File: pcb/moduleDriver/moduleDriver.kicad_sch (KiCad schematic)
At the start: 52 parts, among them J10 Sensor, J11 Power, J12 Power, J7 Sensor, J8 Sensor, J9 Sensor

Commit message: yep, this is the winner
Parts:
- removed D?: WS2812B, LED_SMD:LED_WS2812B_PLCC4_5.0x5.0mm_P3.2mm, symbol LED:WS2812B
- removed D?: LED, LED_SMD:LED_0603_1608Metric, symbol Device:LED_Small
- removed J? (x4): I2C, Connector_PinHeader_2.54mm:PinHeader_1x03_P2.54mm_Vertical, symbol Connector:Conn_01x03_Male
- removed R? (x16): 4.7k, Resistor_SMD:R_0603_1608Metric, symbol Device:R_Small
- removed R?: 1.2k, Resistor_SMD:R_0603_1608Metric, symbol Device:R_Small
- removed R? (x2): 2.2k, Resistor_SMD:R_0603_1608Metric, symbol Device:R_Small
- removed SW? (x2): SW_DIP_x08, symbol Switch:SW_DIP_x08
- added D?: LED, LED_SMD:LED_0603_1608Metric, symbol Device:LED_Small
- added J? (x2): I2C, Connector_PinHeader_2.54mm:PinHeader_1x03_P2.54mm_Vertical, symbol Connector:Conn_01x03_Male
- added R?: 1.2k, Resistor_SMD:R_0603_1608Metric, symbol Device:R_Small
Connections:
- net I2C_PULLUP is gone; now on net URART_LR_TX: U?.26 (GPIO20)
- net SCL is gone; now on net UART_RL_RX: U?.25 (GPIO19)
- net SDA is gone; now on net UART_LR_RX: U?.24 (GPIO18)
- net GND: now also D?.1 (K), J?.1 (Pin_1), J?.1 (Pin_1)
- net UART_LR_RX: now also J?.3 (Pin_3)
- net UART_RL_RX: now also J?.2 (Pin_2)
- net UART_RL_TX: now also U?.22 (GPIO17), J?.2 (Pin_2)
- net URART_LR_TX: now also J?.3 (Pin_3)
- net at U?.27 (GPIO21): now also R?.1
- new net: D?.2 (A), R?.2
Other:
- note added: "UART to other modules"
- note removed: "I hate the DIP switches... How about we use a serially chained UART instead of I2C. Or for that matter, use exactly the neopixel protocol! Each module shows up as a neopixel! Ooh, I like it. That way you can not only chain these modules together, but interchageably sequence together neopixels and displays :-) Back to needing 3.3 <-> 5V voltage level translation, but it's kinda neat Hmmmm... but t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"
- note removed: "I think this is the winning strategy"
- note removed: "I2C to other modules"
- note removed: "MASTER SELECT"
- note removed: "MODULE SELECT"
- note removed: "One module should be set to address 0 via the DIP switches. The master module will turn on GPIO20 (I2C_PULLUP), to power the I2C bus. All other modules will have I2C_PULLUP in a High-Z state"
- note removed: "Or... do this with UARTS"
- note removed: "other options instead of DIP switches:"
- moved on the sheet: H1, H3

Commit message: checking voltage levels. Everythign looks correct
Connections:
- net UART_LR_RX: now also U?.26 (GPIO20); no longer U?.24 (GPIO18)
- net UART_RL_RX: now also U?.22 (GPIO17); no longer U?.25 (GPIO19)
- net UART_RL_TX: now also U?.25 (GPIO19); no longer U?.22 (GPIO17)
- net URART_LR_TX: now also U?.24 (GPIO18); no longer U?.26 (GPIO20)
- net LED: now reaches R?.1, U?.27 (GPIO21)
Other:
- note added: "The 2803 says "for 5V CMOS", but the datasheet says anything more than 2.8V is "on" so we should be good. Hi-z or LOW is OFF > 2.8V is ON"
- note added: "The PICO that doesn't receive anything on UART_LR_RX is the master. Benefits: * zero hardware configuration. The start of the chain automatically the master * the signal is rebuffered at each module. * push-push drivers -- not reliant on pullups, which can receive noise a little more than push-push drivers"
- note removed: "Requires 2 TX uarts on the PICO and 2 RX uarts on the PICO. Also, The PICO that doesn't receive anything on UART_LR_RX is the master. Benefits: * zero hardware configuration. The start of the chain automatically the master * the signal is rebuffered at each module. * push-push drivers -- not reliant on pullups, which can receive noise a little more than push-push drivers"
- moved on the sheet: D?, J?, R?, U?

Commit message: Restarting layout
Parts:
- U1: renamed from U?; footprint Package_TO_SOT_SMD:TO-252-3_TabPin2 -> Package_TO_SOT_SMD:TO-252-2; Comment (none) -> Extended; LCSC# (none) -> C83632
- U2: renamed from U?; Comment (none) -> -
- U3, U4: renamed from U?; footprint (none) -> Package_SO:SOP-18_7x12.5mm_P1.27mm; Comment (none) -> Extended; LCSC# (none) -> C181731
- gave numbers to parts that had none: 13
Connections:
- no-connect marks 0 -> 7
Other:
- moved on the sheet: C4

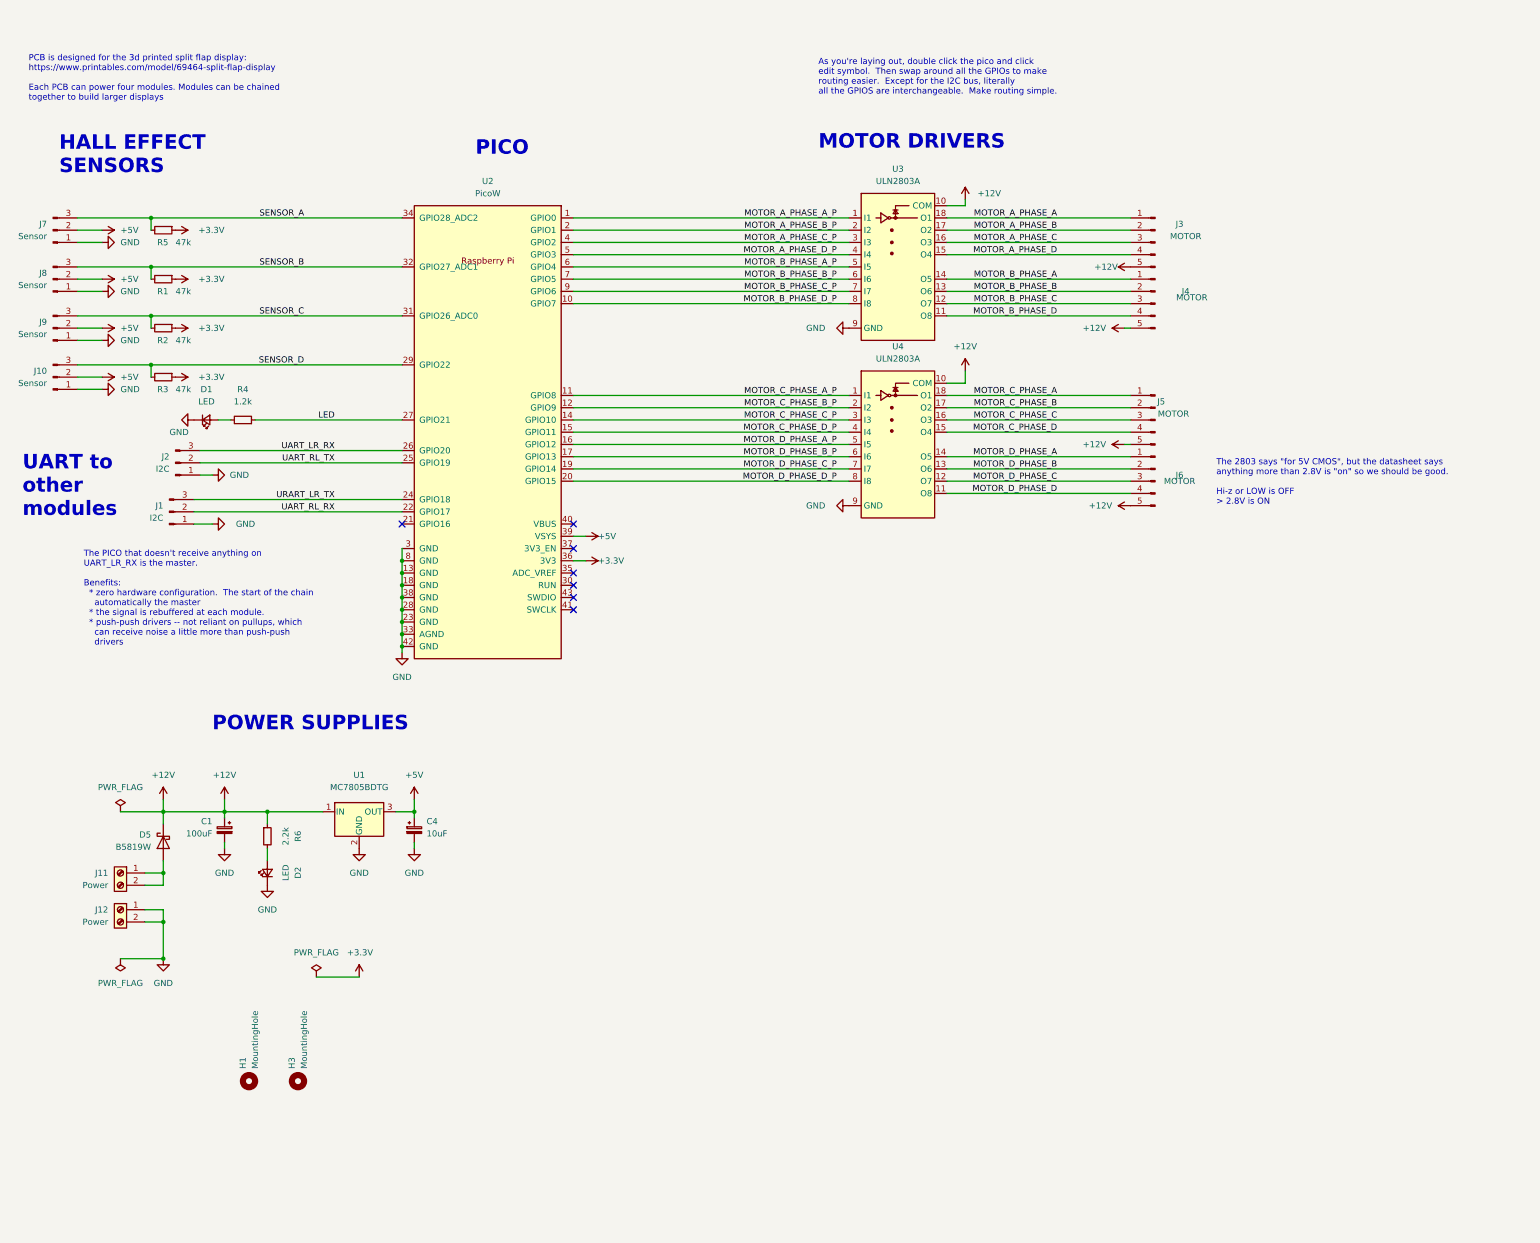
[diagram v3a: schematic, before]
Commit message: Initial layout for new schematic
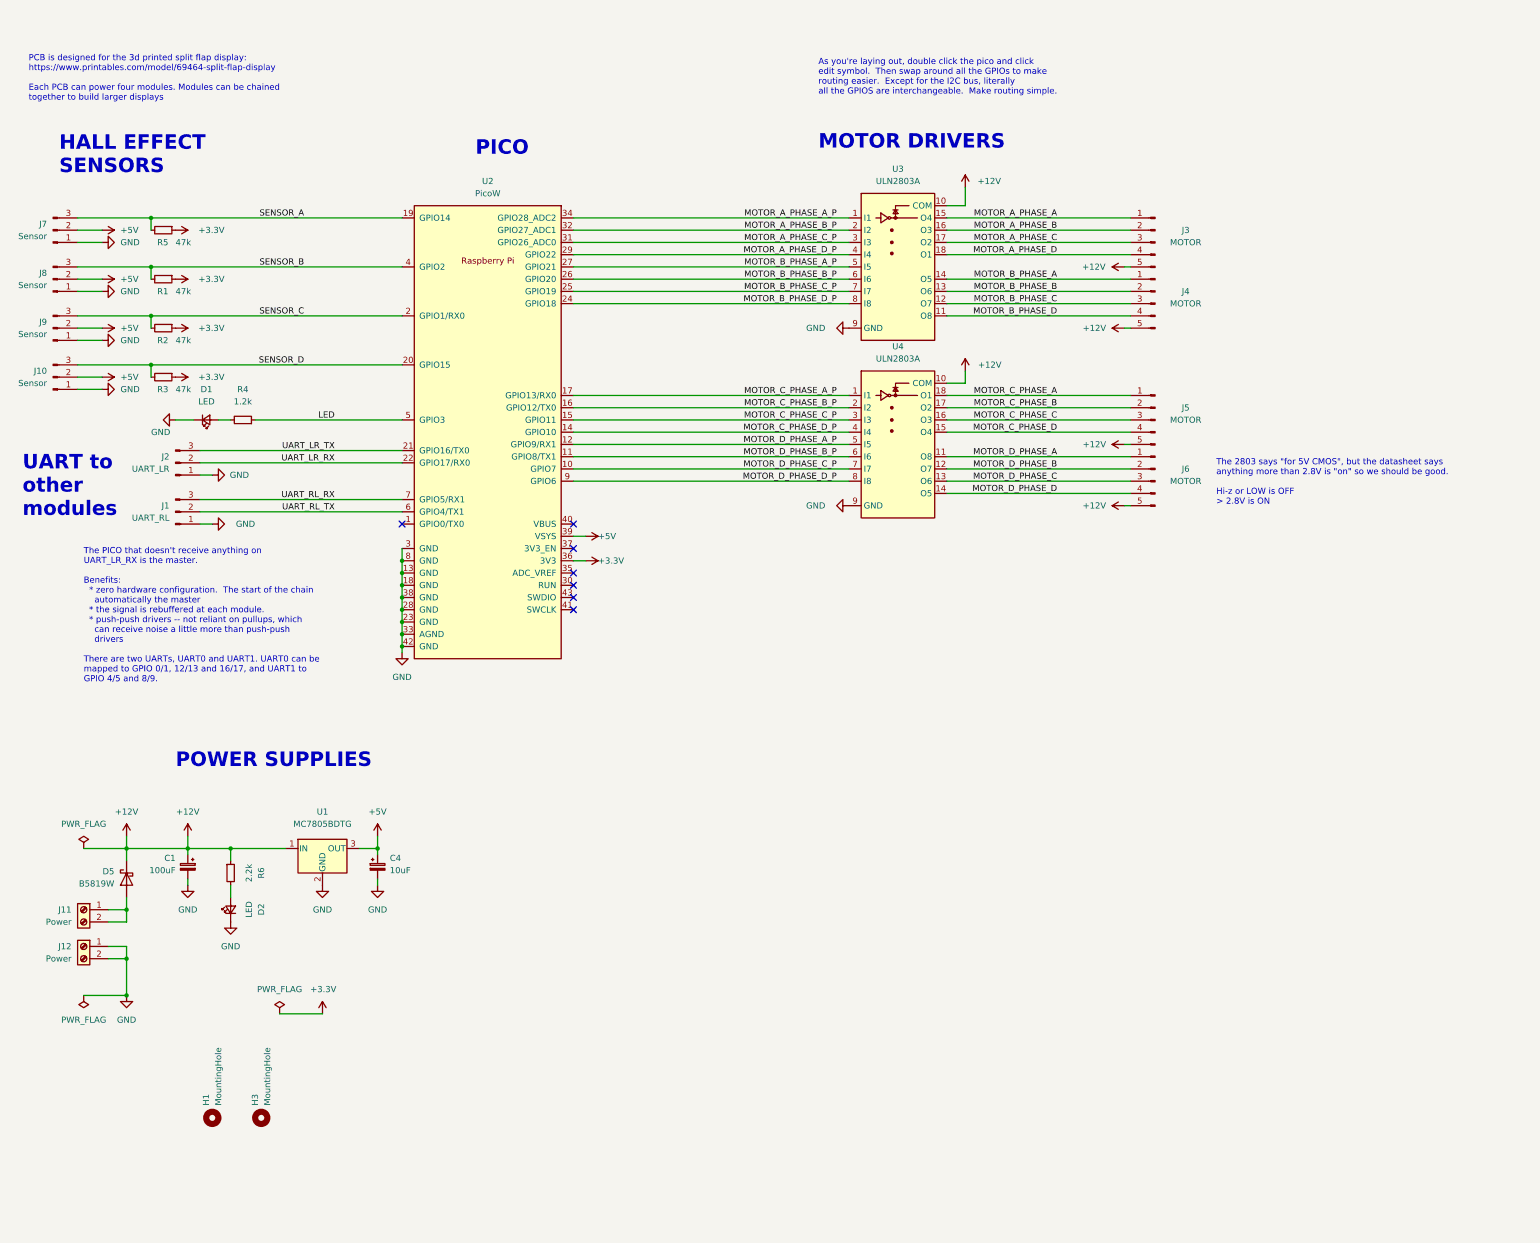
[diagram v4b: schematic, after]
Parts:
- J1: value I2C -> UART_RL
- J2: value I2C -> UART_LR
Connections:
- net LED: now also U2.5 (GPIO3); no longer U2.27 (GPIO21)
- net MOTOR_A_PHASE_A: now also U3.15 (O4); no longer U3.18 (O1)
- net MOTOR_A_PHASE_A_P: now also U2.34 (GPIO28_ADC2); no longer U2.1 (GPIO0)
- net MOTOR_A_PHASE_B: now also U3.16 (O3); no longer U3.17 (O2)
- net MOTOR_A_PHASE_B_P: now also U2.32 (GPIO27_ADC1); no longer U2.2 (GPIO1)
- net MOTOR_A_PHASE_C: now also U3.17 (O2); no longer U3.16 (O3)
- net MOTOR_A_PHASE_C_P: now also U2.31 (GPIO26_ADC0); no longer U2.4 (GPIO2)
- net MOTOR_A_PHASE_D: now also U3.18 (O1); no longer U3.15 (O4)
- net MOTOR_A_PHASE_D_P: now also U2.29 (GPIO22); no longer U2.5 (GPIO3)
- net MOTOR_B_PHASE_A_P: now also U2.27 (GPIO21); no longer U2.6 (GPIO4)
- net MOTOR_B_PHASE_B_P: now also U2.26 (GPIO20); no longer U2.7 (GPIO5)
- net MOTOR_B_PHASE_C_P: now also U2.25 (GPIO19); no longer U2.9 (GPIO6)
- net MOTOR_B_PHASE_D_P: now also U2.24 (GPIO18); no longer U2.10 (GPIO7)
- net MOTOR_C_PHASE_A_P: now also U2.17 (GPIO13/RX0); no longer U2.11 (GPIO8)
- net MOTOR_C_PHASE_B_P: now also U2.16 (GPIO12/TX0); no longer U2.12 (GPIO9)
- net MOTOR_C_PHASE_C_P: now also U2.15 (GPIO11); no longer U2.14 (GPIO10)
- net MOTOR_C_PHASE_D_P: now also U2.14 (GPIO10); no longer U2.15 (GPIO11)
- net MOTOR_D_PHASE_A: now also U4.11 (O8); no longer U4.14 (O5)
- net MOTOR_D_PHASE_A_P: now also U2.12 (GPIO9/RX1); no longer U2.16 (GPIO12)
- net MOTOR_D_PHASE_B: now also U4.12 (O7); no longer U4.13 (O6)
- net MOTOR_D_PHASE_B_P: now also U2.11 (GPIO8/TX1); no longer U2.17 (GPIO13)
- net MOTOR_D_PHASE_C: now also U4.13 (O6); no longer U4.12 (O7)
- net MOTOR_D_PHASE_C_P: now also U2.10 (GPIO7); no longer U2.19 (GPIO14)
- net MOTOR_D_PHASE_D: now also U4.14 (O5); no longer U4.11 (O8)
- net MOTOR_D_PHASE_D_P: now also U2.9 (GPIO6); no longer U2.20 (GPIO15)
- net SENSOR_A: now also U2.19 (GPIO14); no longer U2.34 (GPIO28_ADC2)
- net SENSOR_B: now also U2.4 (GPIO2); no longer U2.32 (GPIO27_ADC1)
- net SENSOR_C: now also U2.2 (GPIO1/RX0); no longer U2.31 (GPIO26_ADC0)
- net SENSOR_D: now also U2.20 (GPIO15); no longer U2.29 (GPIO22)
- net UART_LR_RX: now also J2.2 (Pin_2), U2.22 (GPIO17/RX0); no longer J2.3 (Pin_3), U2.26 (GPIO20)
- net UART_RL_RX: now also J1.3 (Pin_3), U2.7 (GPIO5/RX1); no longer J1.2 (Pin_2), U2.22 (GPIO17)
- net UART_RL_TX: now also J1.2 (Pin_2), U2.6 (GPIO4/TX1); no longer J2.2 (Pin_2), U2.25 (GPIO19)
- net UART_LR_TX: now reaches U2.21 (GPIO16/TX0)
- net UART_LR_TX: now also J2.3 (Pin_3)
- removed net URART_LR_TX: J1.3 (Pin_3), U2.24 (GPIO18)
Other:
- note added: "The PICO that doesn't receive anything on UART_LR_RX is the master. Benefits: * zero hardware configuration. The start of the chain automatically the master * the signal is rebuffered at each module. * push-push drivers -- not reliant on pullups, which can receive noise a little more than push-push drivers There are two UARTs, UART0 and UART1. UART0 can be mapped to GPIO 0/1, 12/13 and 16/17, and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"
- note removed: "The PICO that doesn't receive anything on UART_LR_RX is the master. Benefits: * zero hardware configuration. The start of the chain automatically the master * the signal is rebuffered at each module. * push-push drivers -- not reliant on pullups, which can receive noise a little more than push-push drivers"
- moved on the sheet: C1, C4, D2, D5, H1, H3, J1, J11, J12, R6, U1

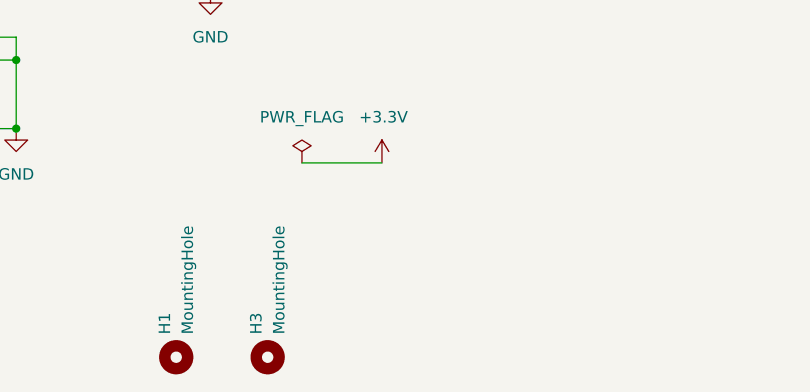
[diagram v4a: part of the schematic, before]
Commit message: Add mounting holes and fix silkscreen
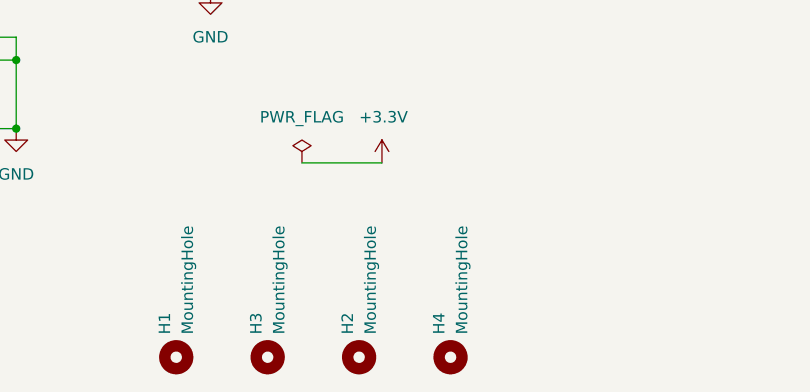
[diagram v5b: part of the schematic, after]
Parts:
- added H2, H4: MountingHole, MountingHole:MountingHole_3.2mm_M3_ISO7380, symbol Mechanical:MountingHole
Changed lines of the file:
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@@
     (pin "1")
+  )
+  (symbol (lib_id "Mechanical:MountingHole") (at 93.98 245.11 90) (unit 1)
+    (in_bom yes) (on_board yes) (fields_autoplaced)
+    (property "Reference" "H4" (id 0) (at 92.7099 242.57 0)
+      (effects (font (size 1.27 1.27)) (justify left))
+    )
+    (property "Value" "MountingHole" (id 1) (at 95.2499 242.57 0)
+      (effects (font (size 1.27 1.27)) (justify left))
+    )
+    (property "Footprint" "MountingHole:MountingHole_3.2mm_M3_ISO7380" (id 2) (at 93.98 245.11 0)
+      (effects (font (size 1.27 1.27)) hide)
+    )
+    (property "Datasheet" "~" (id 3) (at 93.98 245.11 0)
+      (effects (font (size 1.27 1.27)) hide)
+    )
+    (property "Comment" "-" (id 4) (at 93.98 245.11 0)
+      (effects (font (size 1.27 1.27)) hide)
+    )
   )
   (symbol (lib_id "Device:R_Small") (at 53.34 60.96 270) (unit 1)
@@
     (pin "1")
     (pin "2")
+  )
+  (symbol (lib_id "Mechanical:MountingHole") (at 83.82 245.11 90) (unit 1)
+    (in_bom yes) (on_board yes) (fields_autoplaced)
+    (property "Reference" "H2" (id 0) (at 82.5499 242.57 0)
+      (effects (font (size 1.27 1.27)) (justify left))
+    )
+    (property "Value" "MountingHole" (id 1) (at 85.0899 242.57 0)
+      (effects (font (size 1.27 1.27)) (justify left))
+    )
+    (property "Footprint" "MountingHole:MountingHole_3.2mm_M3_ISO7380" (id 2) (at 83.82 245.11 0)
+      (effects (font (size 1.27 1.27)) hide)
+    )
+    (property "Datasheet" "~" (id 3) (at 83.82 245.11 0)
+      (effects (font (size 1.27 1.27)) hide)
+    )
+    (property "Comment" "-" (id 4) (at 83.82 245.11 0)
+      (effects (font (size 1.27 1.27)) hide)
+    )
   )
   (symbol (lib_id "Device:C_Polarized_Small") (at 58.42 193.04 0) (mirror y) (unit 1)
@@
       (reference "H1") (unit 1) (value "MountingHole") (footprint "MountingHole:MountingHole_3.2mm_M3_ISO7380")
     )
+    (path "/2cd9ddec-79bb-4d85-b531-c092512857cd"
+      (reference "H2") (unit 1) (value "MountingHole") (footprint "MountingHole:MountingHole_3.2mm_M3_ISO7380")
+    )
     (path "/ada26385-a60b-45ef-94cb-e7206725bdb7"
       (reference "H3") (unit 1) (value "MountingHole") (footprint "MountingHole:MountingHole_3.2mm_M3_ISO7380")
     )
+    (path "/11666615-58fa-42bb-9293-9cc7bfae59de"
+      (reference "H4") (unit 1) (value "MountingHole") (footprint "MountingHole:MountingHole_3.2mm_M3_ISO7380")
+    )
     (path "/0989f773-d511-4c53-84c7-d6d1f2de1a8e"
